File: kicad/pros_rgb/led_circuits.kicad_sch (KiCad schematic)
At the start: 88 parts, among them U7 MBIA043GP, U8 MBIA043GP, U9 MBIA043GP

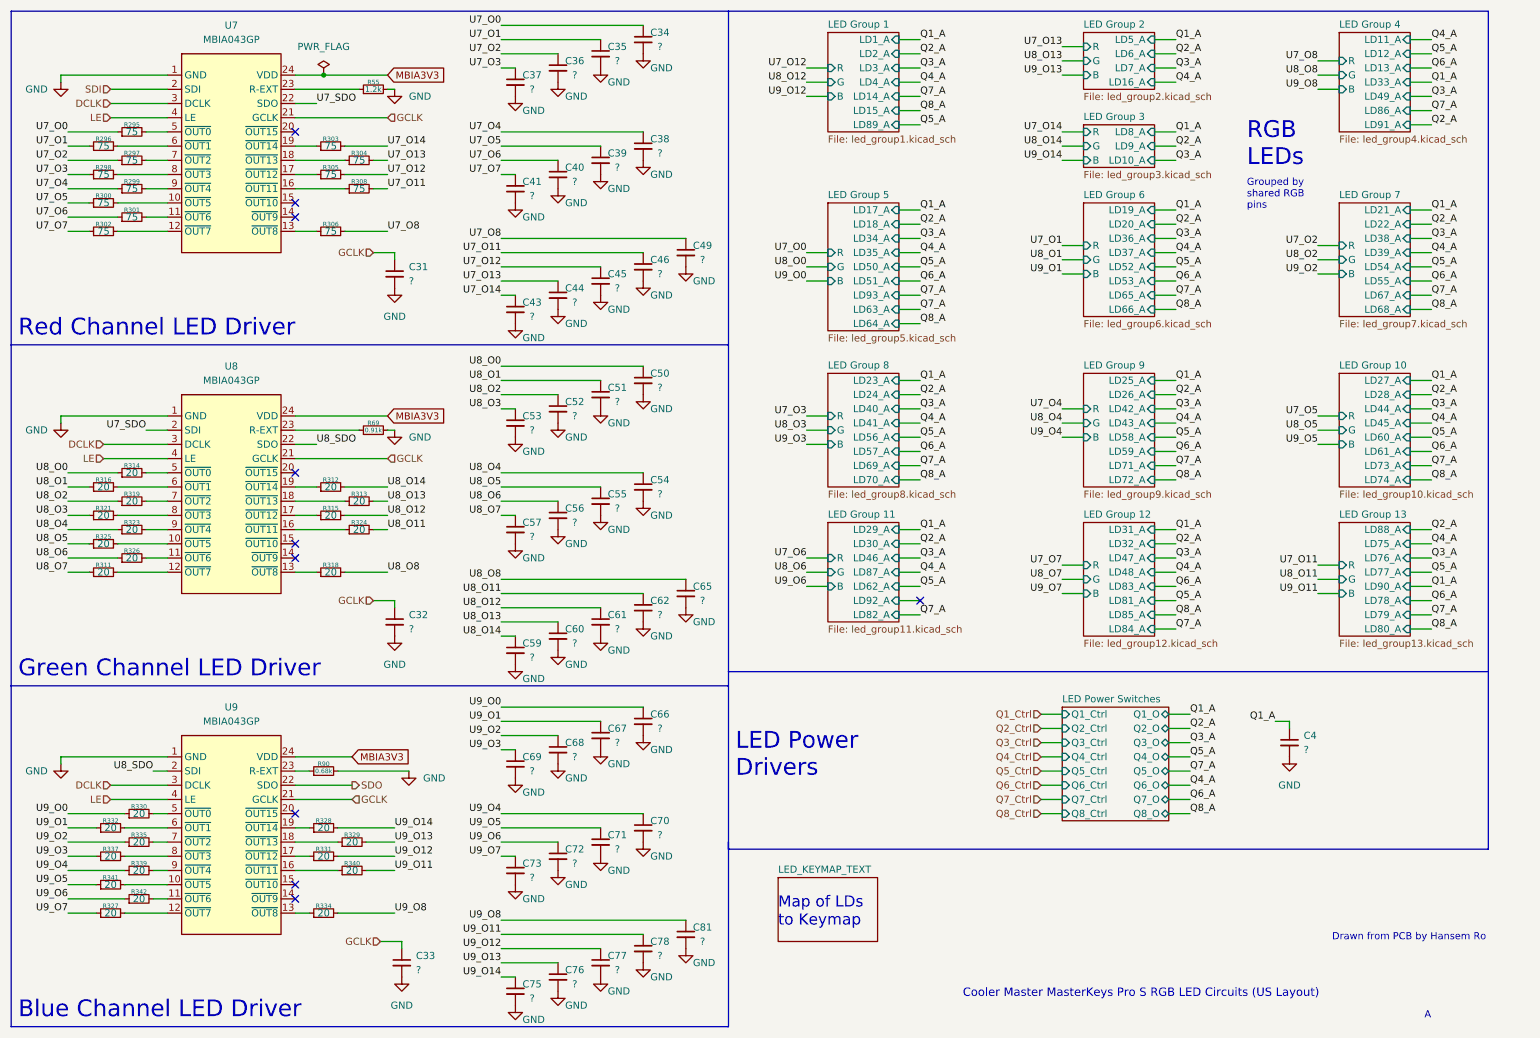
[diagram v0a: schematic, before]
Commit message: kicad/pros_rgb: order led groups by channel number
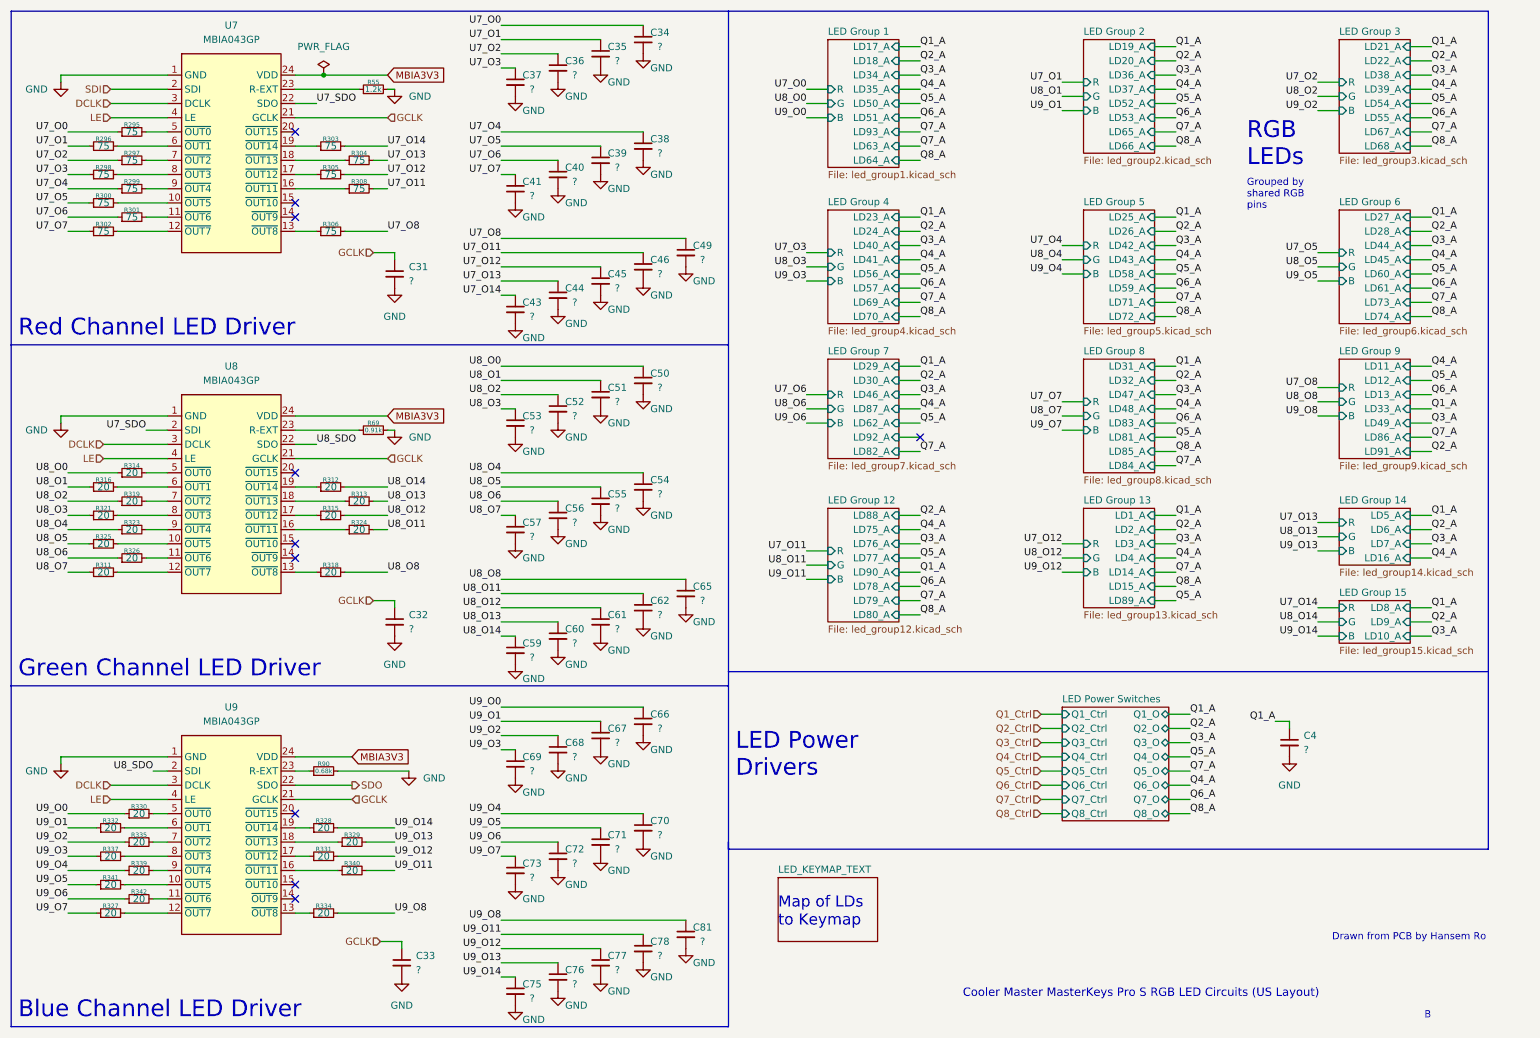
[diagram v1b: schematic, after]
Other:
- removed sheet LED Group 10
- removed sheet LED Group 11
- added sheet LED Group 14 (led_group14.kicad_sch)
- added sheet LED Group 15 (led_group15.kicad_sch)
- sheet LED Group 1 ports: added LD17_A, LD18_A, LD34_A, LD35_A, LD50_A, LD51_A, LD63_A, LD64_A, LD93_A; removed LD14_A, LD15_A, LD1_A, LD2_A, LD3_A, LD4_A, LD89_A
- sheet LED Group 12 ports: added LD75_A, LD76_A, LD77_A, LD78_A, LD79_A, LD80_A, LD88_A, LD90_A; removed LD31_A, LD32_A, LD47_A, LD48_A, LD81_A, LD83_A, LD84_A, LD85_A
- sheet LED Group 13 ports: added LD14_A, LD15_A, LD1_A, LD2_A, LD3_A, LD4_A, LD89_A; removed LD75_A, LD76_A, LD77_A, LD78_A, LD79_A, LD80_A, LD88_A, LD90_A
- sheet LED Group 2 ports: added LD19_A, LD20_A, LD36_A, LD37_A, LD52_A, LD53_A, LD65_A, LD66_A; removed LD16_A, LD5_A, LD6_A, LD7_A
- sheet LED Group 3 ports: added LD21_A, LD22_A, LD38_A, LD39_A, LD54_A, LD55_A, LD67_A, LD68_A; removed LD10_A, LD8_A, LD9_A
- sheet LED Group 4 ports: added LD23_A, LD24_A, LD40_A, LD41_A, LD56_A, LD57_A, LD69_A, LD70_A; removed LD11_A, LD12_A, LD13_A, LD33_A, LD49_A, LD86_A, LD91_A
- sheet LED Group 5 ports: added LD25_A, LD26_A, LD42_A, LD43_A, LD58_A, LD59_A, LD71_A, LD72_A; removed LD17_A, LD18_A, LD34_A, LD35_A, LD50_A, LD51_A, LD63_A, LD64_A, LD93_A
- sheet LED Group 6 ports: added LD27_A, LD28_A, LD44_A, LD45_A, LD60_A, LD61_A, LD73_A, LD74_A; removed LD19_A, LD20_A, LD36_A, LD37_A, LD52_A, LD53_A, LD65_A, LD66_A
- sheet LED Group 7 ports: added LD29_A, LD30_A, LD46_A, LD62_A, LD82_A, LD87_A, LD92_A; removed LD21_A, LD22_A, LD38_A, LD39_A, LD54_A, LD55_A, LD67_A, LD68_A
- sheet LED Group 8 ports: added LD31_A, LD32_A, LD47_A, LD48_A, LD81_A, LD83_A, LD84_A, LD85_A; removed LD23_A, LD24_A, LD40_A, LD41_A, LD56_A, LD57_A, LD69_A, LD70_A
- sheet LED Group 9 ports: added LD11_A, LD12_A, LD13_A, LD33_A, LD49_A, LD86_A, LD91_A; removed LD25_A, LD26_A, LD42_A, LD43_A, LD58_A, LD59_A, LD71_A, LD72_A
- note added: "B"
- note removed: "A"
